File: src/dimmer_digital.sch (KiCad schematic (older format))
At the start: 25 parts, among them J2 CONECTOR_LEFT, J3 CONNECTOR_SPEED, J4 TERMINAL_AC, J5 TERMINAL_LOAD, J6 CONECTOR_RIGHT, Q1 TIC226, SW1 SWITCH_SPEED, SW2 SW_Push, U1 ATtiny13A-PU, U2 MOC3021M, U3 4N25

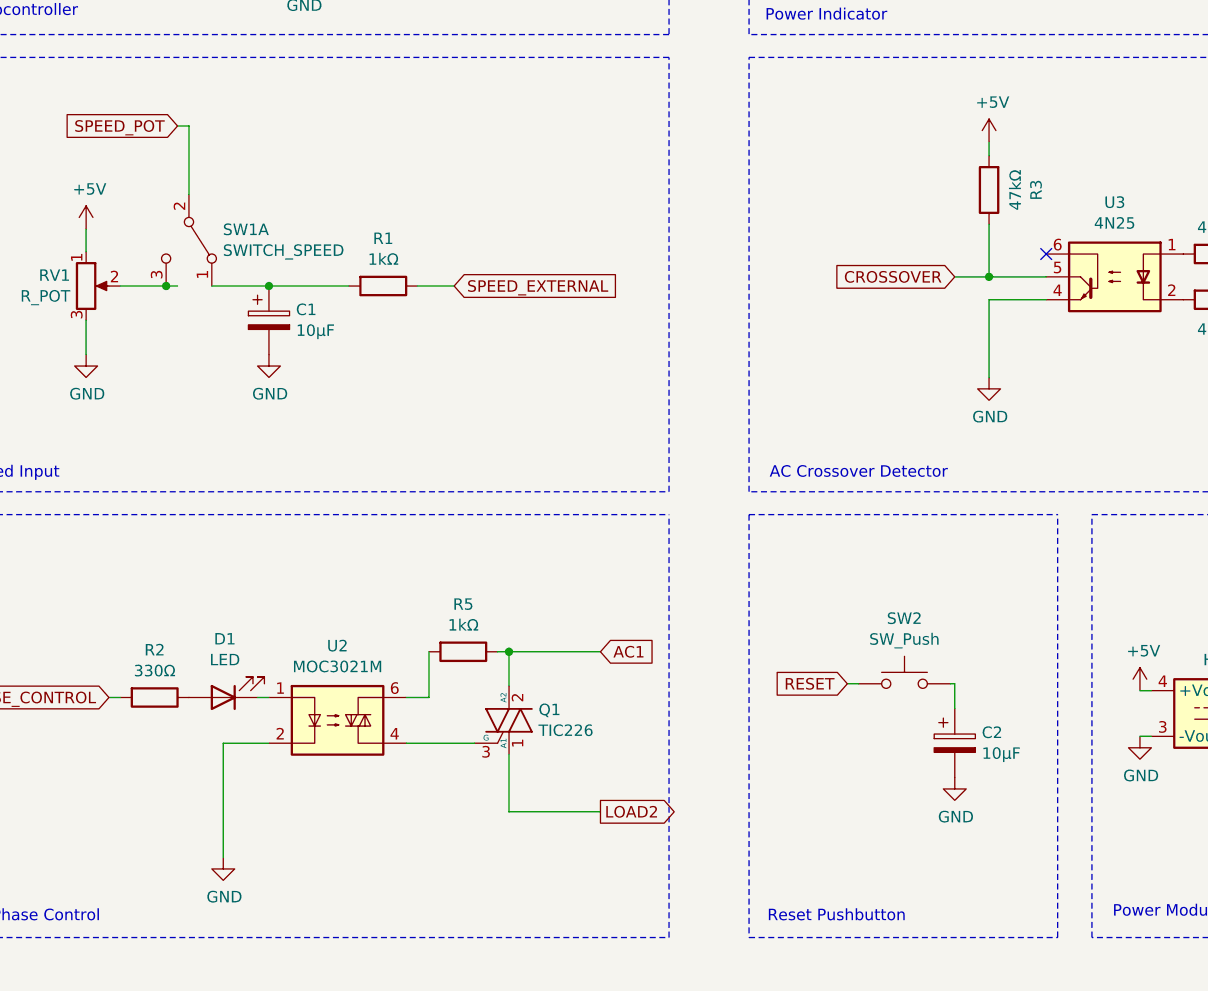
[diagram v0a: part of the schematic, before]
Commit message: Added pullup to reset pin
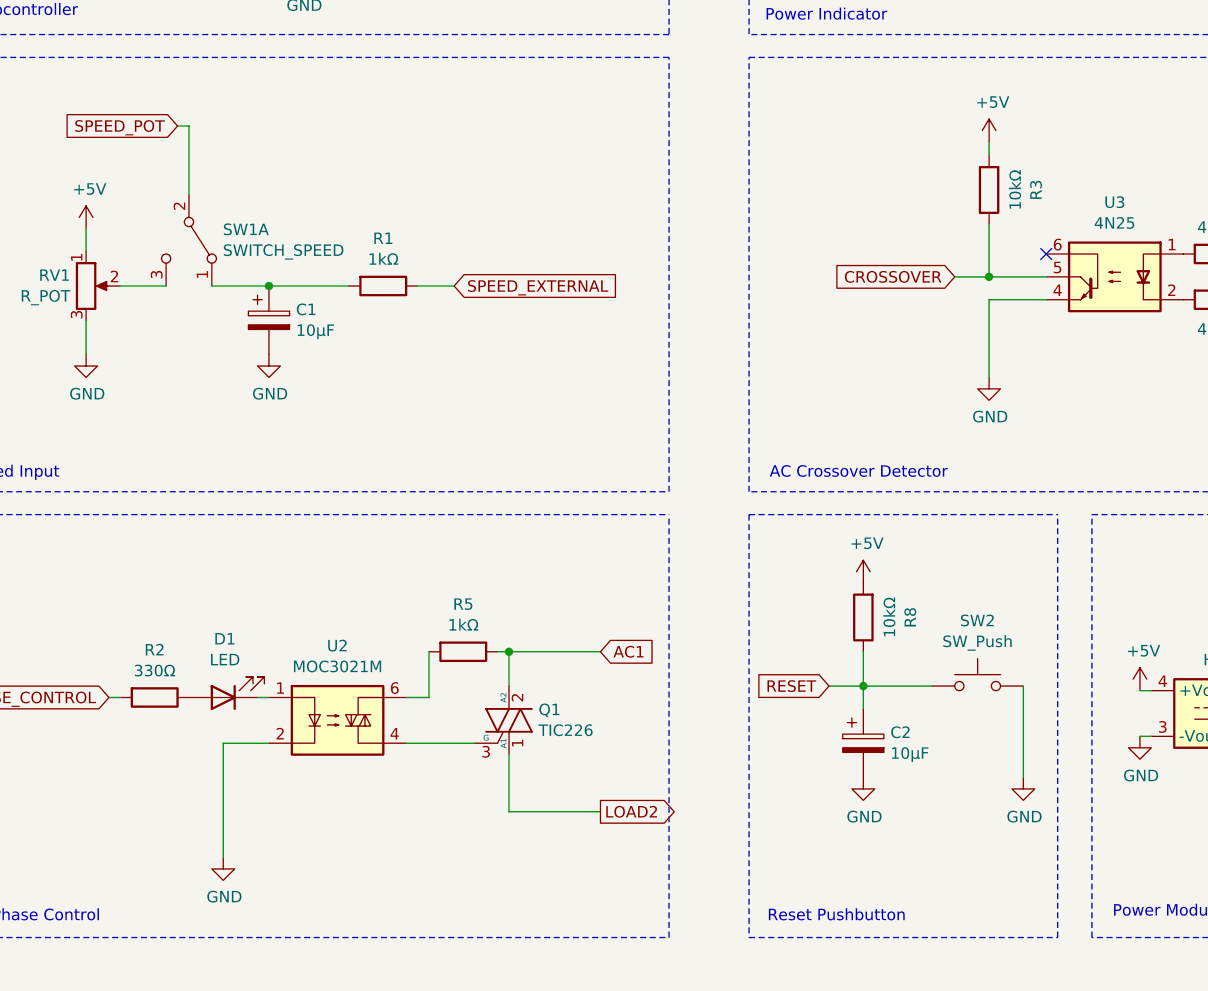
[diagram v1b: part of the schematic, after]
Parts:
- added R8: 10kΩ, Resistor_THT:R_Axial_DIN0207_L6.3mm_D2.5mm_P7.62mm_Horizontal, symbol Device:R
- R3: value 47kΩ -> 10kΩ
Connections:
- net +5V: now also R8.2
- net GND: now also SW2.2
- net RESET: now also C2.1, R8.1
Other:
- moved on the sheet: C2, SW2
